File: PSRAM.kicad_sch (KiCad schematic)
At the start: 4 parts, among them J901 OCTOSPI, U901 S27KL0642DPBHB023

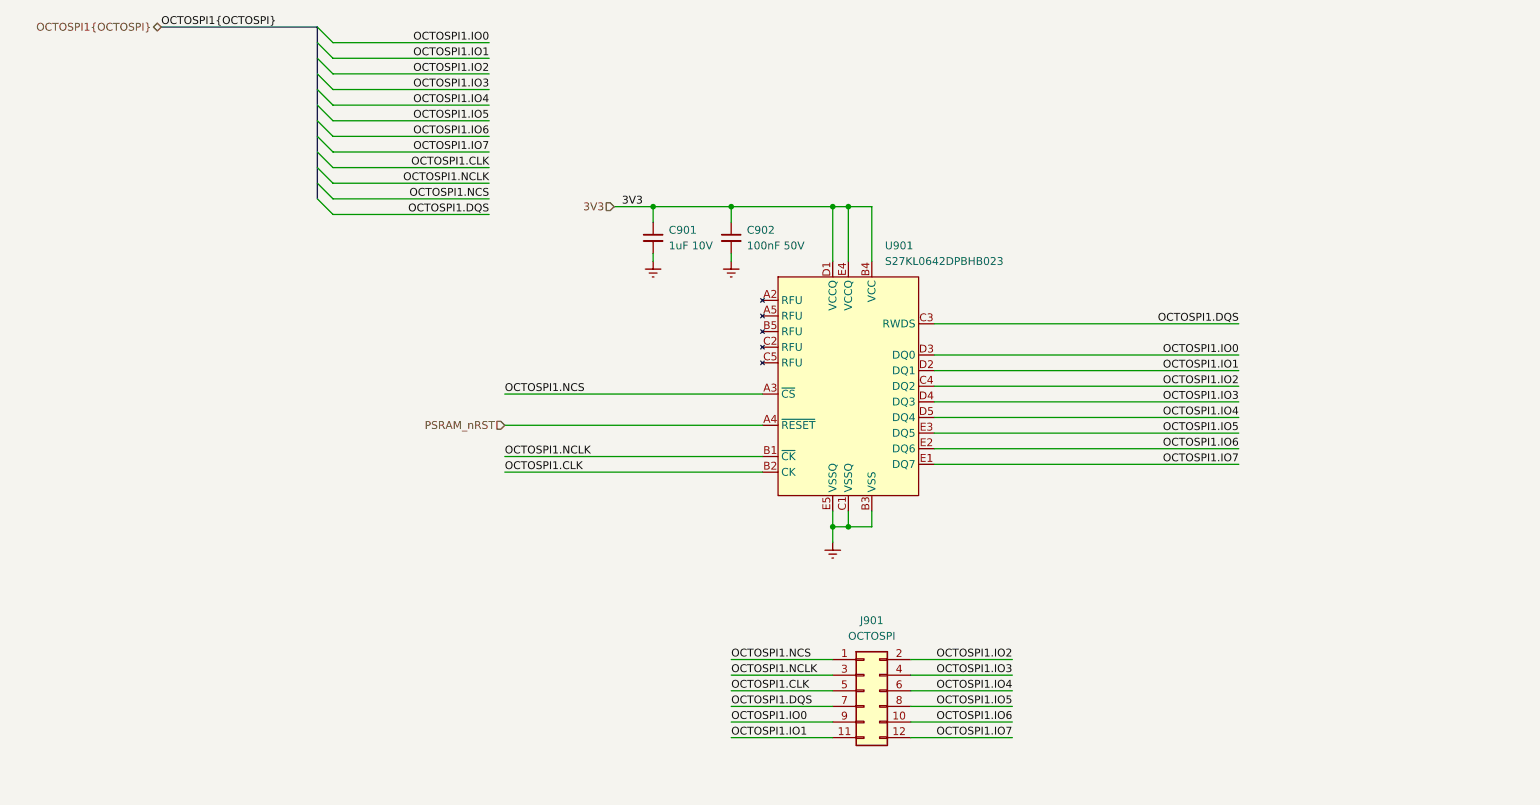
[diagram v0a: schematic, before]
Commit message: subcircuit layout + minor schematic updates
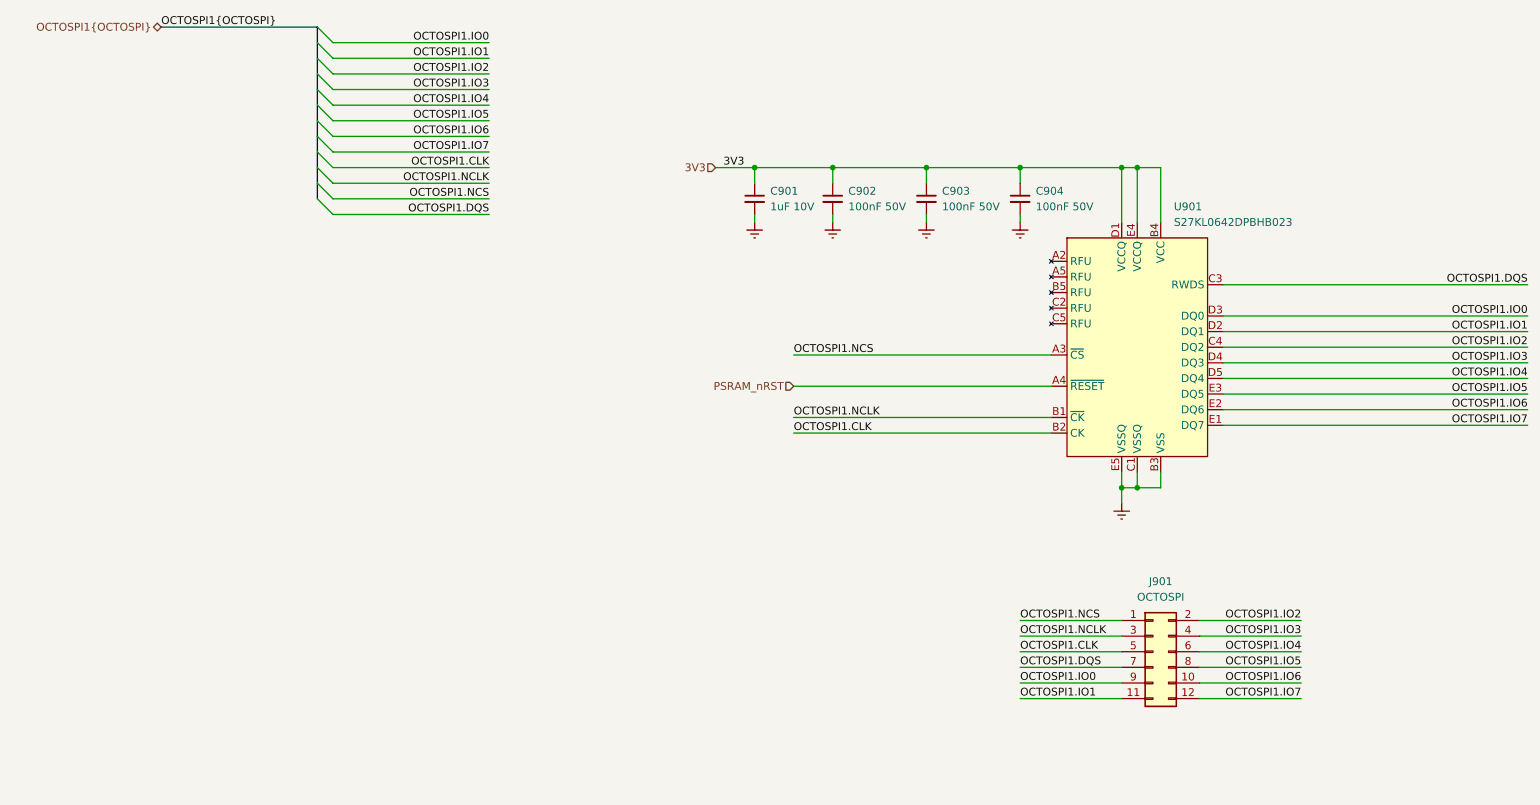
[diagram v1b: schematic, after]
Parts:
- added C903, C904: 100nF 50V, BR_Passives:C_0402_1005Metric-minimized, symbol BR_Capacitors_0402:C_0402_100nF_50V_X7R_10%_AEC-Q200
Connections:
- net 3V3: now also C903.1, C904.1
- net GND: now also C903.2, C904.2
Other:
- moved on the sheet: C901, C902, J901, U901

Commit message: BGA fanout + added SMPS layout
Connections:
- net OCTOSPI1.CLK: now also J901.2 (Pin_2); no longer J901.5 (Pin_5)
- net OCTOSPI1.DQS: now also J901.1 (Pin_1); no longer J901.7 (Pin_7)
- net OCTOSPI1.IO0: now also J901.5 (Pin_5); no longer J901.9 (Pin_9)
- net OCTOSPI1.IO1: now also J901.6 (Pin_6); no longer J901.11 (Pin_9)
- net OCTOSPI1.IO2: now also J901.7 (Pin_7); no longer J901.2 (Pin_2)
- net OCTOSPI1.IO3: now also J901.8 (Pin_8); no longer J901.4 (Pin_4)
- net OCTOSPI1.IO4: now also J901.9 (Pin_9); no longer J901.6 (Pin_6)
- net OCTOSPI1.IO5: now also J901.10 (Pin_10); no longer J901.8 (Pin_8)
- net OCTOSPI1.IO6: now also J901.11 (Pin_9); no longer J901.10 (Pin_10)
- net OCTOSPI1.NCLK: now also J901.4 (Pin_4); no longer J901.3 (Pin_3)
- net OCTOSPI1.NCS: now also J901.3 (Pin_3); no longer J901.1 (Pin_1)

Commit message: last checks + board characteristics tables
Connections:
- net OCTOSPI1.CLK renamed OCTOSPI1.CLK+
- net OCTOSPI1.NCLK renamed OCTOSPI1.CLK-
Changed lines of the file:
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@@
 		)
 	)
-	(label "OCTOSPI1.CLK"
+	(label "OCTOSPI1.CLK+"
 		(at 224.79 121.92 180)
 		(effects
@@
 		)
 	)
-	(label "OCTOSPI1.NCLK"
+	(label "OCTOSPI1.CLK-"
 		(at 224.79 124.46 180)
 		(effects
@@
 		)
 	)
-	(label "OCTOSPI1.CLK"
+	(label "OCTOSPI1.CLK+"
 		(at 92.71 48.26 180)
 		(effects
@@
 		)
 	)
-	(label "OCTOSPI1.NCLK"
+	(label "OCTOSPI1.CLK-"
 		(at 92.71 50.8 180)
 		(effects
@@
 		)
 	)
-	(label "OCTOSPI1.CLK"
+	(label "OCTOSPI1.CLK+"
 		(at 142.24 91.44 0)
 		(effects
@@
 		)
 	)
-	(label "OCTOSPI1.NCLK"
+	(label "OCTOSPI1.CLK-"
 		(at 142.24 88.9 0)
 		(effects
@@
 		)
 	)
+	(netclass_flag ""
+		(length 2.54)
+		(shape round)
+		(at 224.79 121.92 270)
+		(effects
+			(font
+				(size 1.27 1.27)
+			)
+			(justify right bottom)
+		)
+		(property "Netclass" "OCTOSPI"
+			(at 228.092 121.92 0)
+			(effects
+				(font
+					(size 1.27 1.27)
+				)
+				(justify left)
+			)
+		)
+		(property "Component Class" ""
+			(at -67.31 5.08 0)
+			(effects
+				(font
+					(size 1.27 1.27)
+					(italic yes)
+				)
+			)
+		)
+	)
+	(netclass_flag ""
+		(length 2.54)
+		(shape round)
+		(at 224.79 124.46 270)
+		(effects
+			(font
+				(size 1.27 1.27)
+			)
+			(justify right bottom)
+		)
+		(property "Netclass" "OCTOSPI"
+			(at 228.092 124.46 0)
+			(effects
+				(font
+					(size 1.27 1.27)
+				)
+				(justify left)
+			)
+		)
+		(property "Component Class" ""
+			(at -5.08 -1.27 0)
+			(effects
+				(font
+					(size 1.27 1.27)
+					(italic yes)
+				)
+			)
+		)
+	)

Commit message: Rev A release files
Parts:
- C901: JLCPCB Part Num C528974 -> C23692972
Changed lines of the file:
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@@
 			)
 		)
-		(property "JLCPCB Part Num" "C528974"
+		(property "JLCPCB Part Num" "C23692972"
 			(at 135.89 7.62 0)
 			(effects

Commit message: fixing JLC rules
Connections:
- net OCTOSPI1.CLK+: now also J901.4 (Pin_4); no longer J901.2 (Pin_2)
- net OCTOSPI1.CLK-: now also J901.2 (Pin_2); no longer J901.4 (Pin_4)
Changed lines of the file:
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@@
 	)
 	(label "OCTOSPI1.CLK+"
-		(at 224.79 121.92 180)
+		(at 224.79 124.46 180)
 		(effects
 			(font
@@
 	)
 	(label "OCTOSPI1.CLK-"
-		(at 224.79 124.46 180)
+		(at 224.79 121.92 180)
 		(effects
 			(font

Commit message: refactoring tx a bit
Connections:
- net OCTOSPI1.IO0: now also J901.6 (Pin_6); no longer J901.5 (Pin_5)
- net OCTOSPI1.IO1: now also J901.8 (Pin_8); no longer J901.6 (Pin_6)
- net OCTOSPI1.IO2: now also J901.5 (Pin_5); no longer J901.7 (Pin_7)
- net OCTOSPI1.IO3: now also J901.7 (Pin_7); no longer J901.8 (Pin_8)
- net OCTOSPI1.IO4: now also J901.10 (Pin_10); no longer J901.9 (Pin_9)
- net OCTOSPI1.IO5: now also J901.9 (Pin_9); no longer J901.10 (Pin_10)
- net OCTOSPI1.IO6: now also J901.12 (Pin_9); no longer J901.11 (Pin_9)
- net OCTOSPI1.IO7: now also J901.11 (Pin_9); no longer J901.12 (Pin_9)
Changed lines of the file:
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@@
 	)
 	(label "OCTOSPI1.IO5"
-		(at 224.79 132.08 180)
-		(effects
-			(font
-				(size 1.27 1.27)
-			)
-			(justify right bottom)
+		(at 179.07 132.08 0)
+		(effects
+			(font
+				(size 1.27 1.27)
+			)
+			(justify left bottom)
 		)
 	)
@@
 	)
 	(label "OCTOSPI1.IO6"
-		(at 179.07 134.62 0)
-		(effects
-			(font
-				(size 1.27 1.27)
-			)
-			(justify left bottom)
+		(at 224.79 134.62 180)
+		(effects
+			(font
+				(size 1.27 1.27)
+			)
+			(justify right bottom)
 		)
 	)
@@
 	)
 	(label "OCTOSPI1.IO1"
-		(at 224.79 127 180)
+		(at 224.79 129.54 180)
 		(effects
 			(font
@@
 	)
 	(label "OCTOSPI1.IO4"
-		(at 179.07 132.08 0)
-		(effects
-			(font
-				(size 1.27 1.27)
-			)
-			(justify left bottom)
+		(at 224.79 132.08 180)
+		(effects
+			(font
+				(size 1.27 1.27)
+			)
+			(justify right bottom)
 		)
 	)
 	(label "OCTOSPI1.IO7"
-		(at 224.79 134.62 180)
-		(effects
-			(font
-				(size 1.27 1.27)
-			)
-			(justify right bottom)
+		(at 179.07 134.62 0)
+		(effects
+			(font
+				(size 1.27 1.27)
+			)
+			(justify left bottom)
 		)
 	)
@@
 	)
 	(label "OCTOSPI1.IO2"
-		(at 179.07 129.54 0)
+		(at 179.07 127 0)
 		(effects
 			(font
@@
 	)
 	(label "OCTOSPI1.IO3"
-		(at 224.79 129.54 180)
-		(effects
-			(font
-				(size 1.27 1.27)
-			)
-			(justify right bottom)
+		(at 179.07 129.54 0)
+		(effects
+			(font
+				(size 1.27 1.27)
+			)
+			(justify left bottom)
 		)
 	)
@@
 	)
 	(label "OCTOSPI1.IO0"
-		(at 179.07 127 0)
-		(effects
-			(font
-				(size 1.27 1.27)
-			)
-			(justify left bottom)
-		)
-	)
+		(at 224.79 127 180)
+		(effects
+			(font
+				(size 1.27 1.27)
+			)
+			(justify right bottom)
+		)
+	)

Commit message: some last minute tidy up
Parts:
- removed J901: OCTOSPI, BR_Connectors:PinHeader_2x06_P2.54mm_Vertical_SMD, symbol BR_Connectors_Header:Header_Pin_02x06_2.54mm_Vert_SMD
- added J901: FPGA, BR_Connectors:HDR-SMD_20P-P2.54-V-M-R2-C10-S7.5, symbol BR_Connectors_Header:Header_Pin_02x10_2.54mm_Vert_PTH
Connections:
- net 3V3: now also J901.19 (Pin_19)
- net GND: now also J901.20 (Pin_20)
- net OCTOSPI1.CLK+: now also J901.4 (Pin_4)
- net OCTOSPI1.CLK-: now also J901.2 (Pin_2)
- net OCTOSPI1.DQS: now also J901.1 (Pin_1)
- net OCTOSPI1.IO0: now also J901.6 (Pin_6)
- net OCTOSPI1.IO1: now also J901.8 (Pin_8)
- net OCTOSPI1.IO2: now also J901.5 (Pin_5)
- net OCTOSPI1.IO3: now also J901.7 (Pin_7)
- net OCTOSPI1.IO4: now also J901.10 (Pin_10)
- net OCTOSPI1.IO5: now also J901.9 (Pin_9)
- net OCTOSPI1.IO6: now also J901.12 (Pin_12)
- net OCTOSPI1.IO7: now also J901.11 (Pin_11)
- net OCTOSPI1.NCS: now also J901.3 (Pin_3)
- net PSRAM_nRST renamed OCTOSPI1.RST
- net OCTOSPI1.RST: now also J901.14 (Pin_14)
- no-connect marks 0 -> 5
